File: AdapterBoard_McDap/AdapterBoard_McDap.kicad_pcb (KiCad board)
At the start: 2 copper layers, 71.1 x 55.2 mm, 6 parts, among them CN10 CN10, CN7 CN7, J2_J4 LaunchPad, J3_J1 LaunchPad, J5 RSLK2

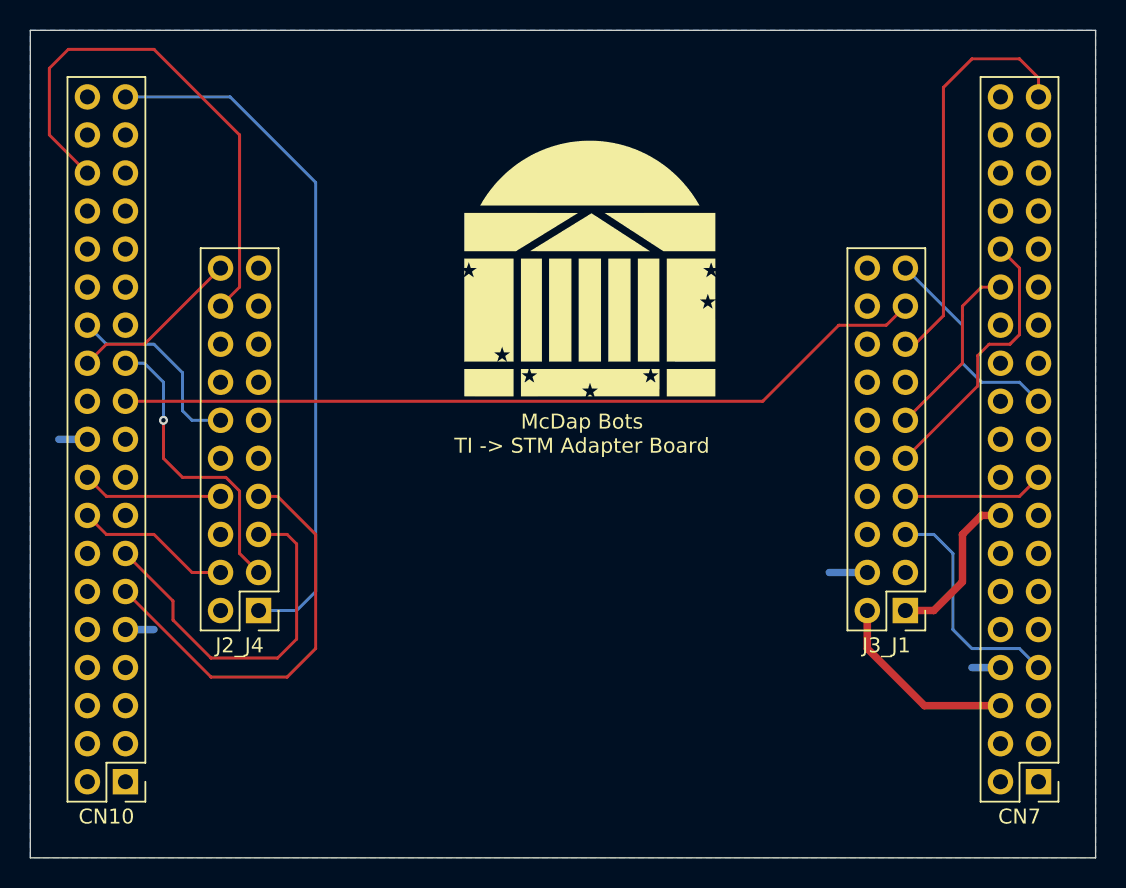
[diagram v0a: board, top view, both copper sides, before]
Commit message: changed pin mappings
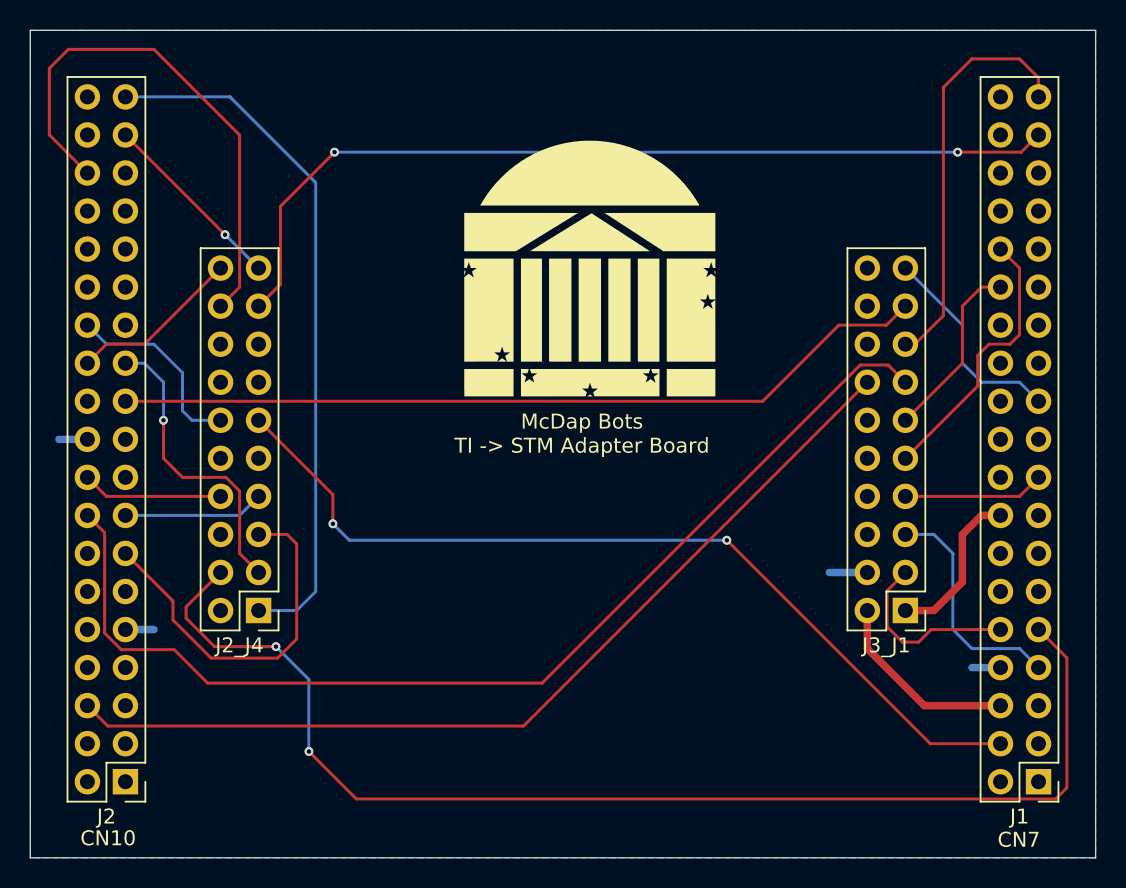
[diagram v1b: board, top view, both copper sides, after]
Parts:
- renumbered CN7 to J1, CN10 to J2
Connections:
- J1 pad 10: PD_1 -> PA25
- J1 pad 35: PC_2 -> PA12
- J1 pad 4: PD_2 -> PB13
- J1 pad 9: PD_0 -> PB12
- J2 pad 11: PA31 -> PA_5
- J2 pad 15: PA_7 -> PA31
- J2 pad 16: PB12 -> PB9
- J2 pad 35: PC_4 -> PA13
- J2 pad 6: PA_3 -> PA24
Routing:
- net PB9: track 0.00 -> 72.4 mm
- net PB12: track 10.5 -> 82.3 mm, vias 0 -> 2
- net PA24: track 0.00 -> 62.1 mm
- net PA12: track 0.00 -> 59.9 mm, vias 0 -> 2
- net PB13: track 0.00 -> 59.6 mm, vias 0 -> 2
- net PA31: track 28.3 -> 9.42 mm
- net PA13: track 0.00 -> 12.6 mm, vias 0 -> 1
- net PA25: track 0.00 -> 12.5 mm
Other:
- board text added: "CN10"
- board text added: "CN7"
